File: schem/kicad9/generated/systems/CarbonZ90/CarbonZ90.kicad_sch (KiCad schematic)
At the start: 0 parts

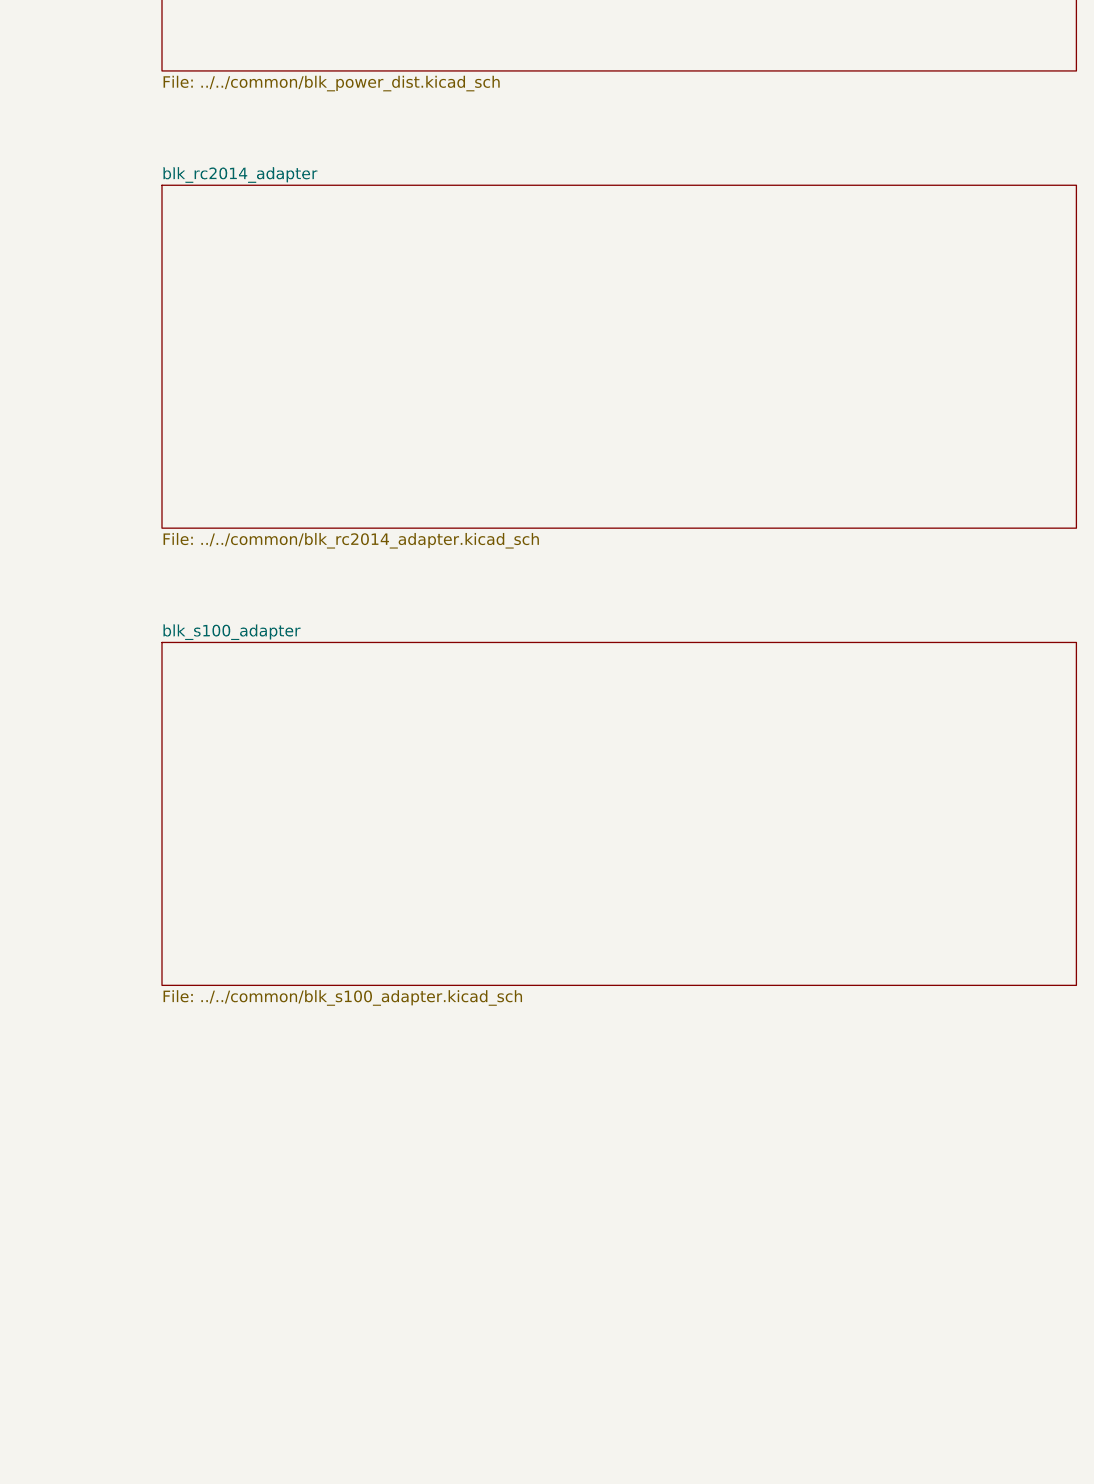
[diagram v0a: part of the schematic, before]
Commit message: kicad: add carbon block symbol library + docs + regen scripts
Detailed description:
- What was implemented: added schem/kicad9/libs/carbon_blocks.kicad_sym placeholder symbols, schem/kicad9/docs/USAGE.md, and scripts/gen_kicad.ps1 plus scripts/gen_kicad.sh; generator now embeds and uses carbon_blocks symbols in generated common block sheets and adds a JTAG/UART common block to system tops.
- Why it exists: keeps the generated hierarchy self-contained and makes regeneration repeatable while reserving a clear path to later map blocks to real parts.
- Architectural assumptions: generator overwrites only schem/kicad9/generated/; carbon_blocks symbols are placeholders (no pin-level mapping in v1); common blocks are represented as simple symbols inside common subsheets.
- How to run it: scripts/gen_kicad.ps1 or scripts/gen_kicad.sh (or python tools/kicadgen/src/kicadgen.py).
- What is NOT implemented yet: automatic mapping to specific 74ACT parts and real footprints, detailed per-net wiring between blocks, and deeper parsing of hdl/spec YAML beyond the mapping specs.
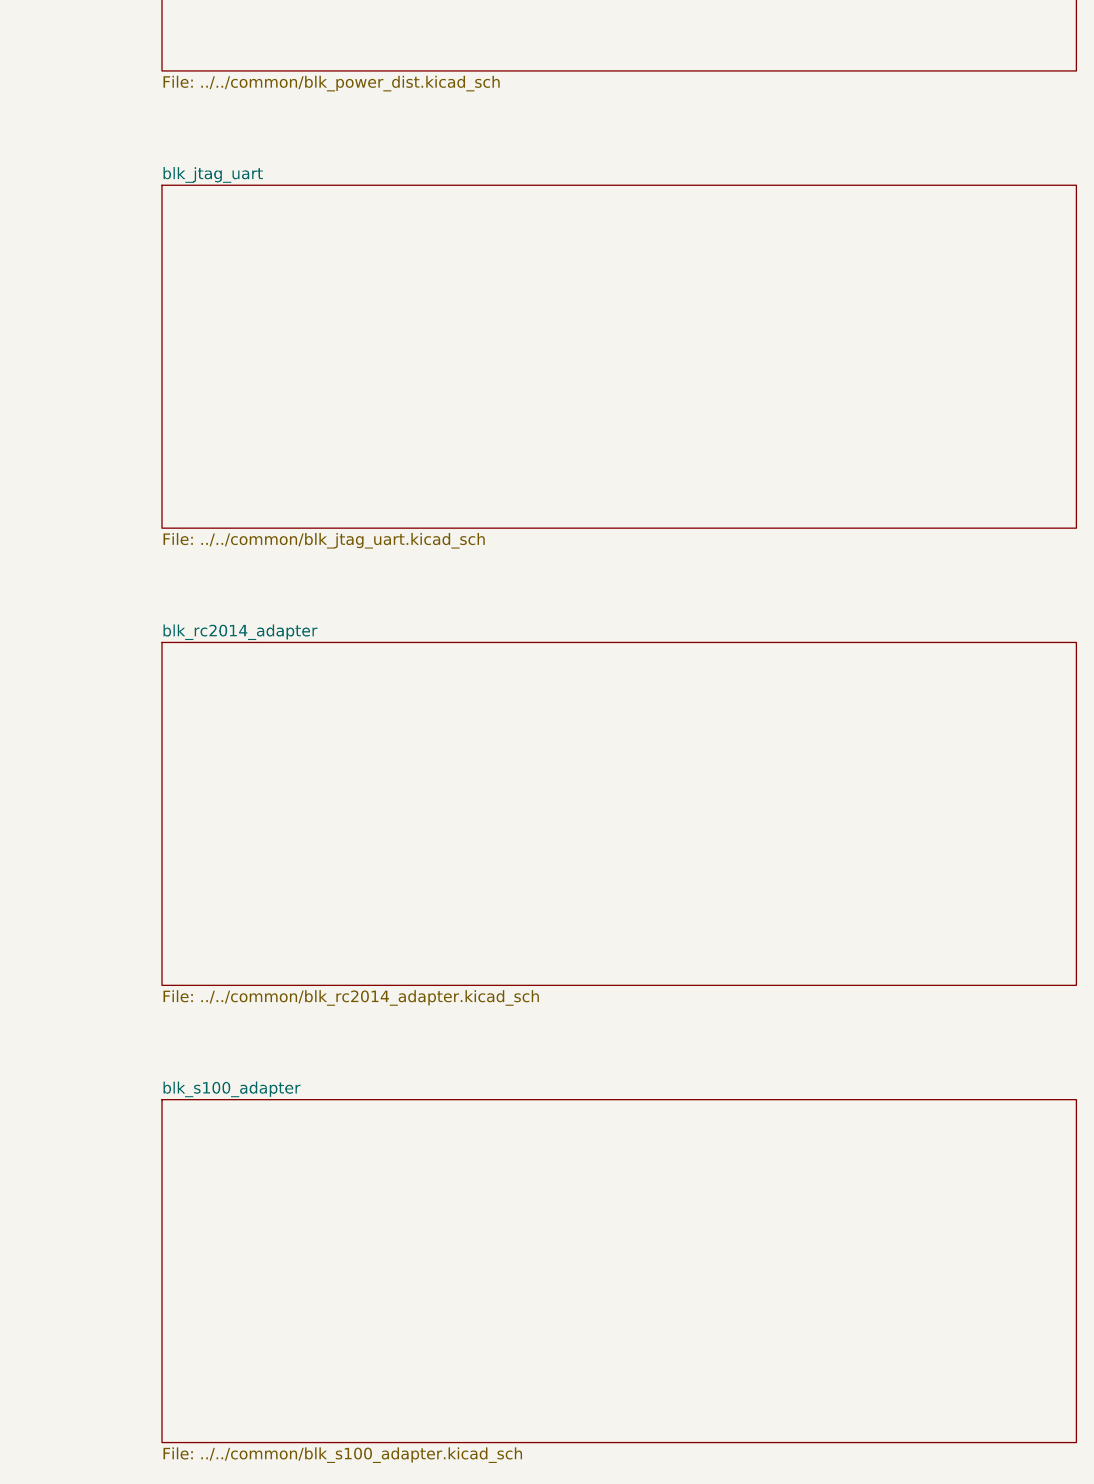
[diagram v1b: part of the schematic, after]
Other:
- added sheet blk_jtag_uart (../../common/blk_jtag_uart.kicad_sch)
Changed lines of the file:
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@@
 		(property
 			"Sheetname"
-			"blk_rc2014_adapter"
+			"blk_jtag_uart"
 			(at
 				139.7
@@
 		(property
 			"Sheetfile"
-			"../../common/blk_rc2014_adapter.kicad_sch"
+			"../../common/blk_jtag_uart.kicad_sch"
 			(at
 				139.7
@@
 		(property
 			"Sheetname"
-			"blk_s100_adapter"
+			"blk_rc2014_adapter"
 			(at
 				139.7
@@
 		(property
 			"Sheetfile"
-			"../../common/blk_s100_adapter.kicad_sch"
+			"../../common/blk_rc2014_adapter.kicad_sch"
 			(at
 				139.7
@@
 				)
 			)
+		)
+	)
+	(sheet
+		(at 139.7 350.52)
+		(size 101.6 38.1)
+		(exclude_from_sim no)
+		(in_bom yes)
+		(on_board yes)
+		(dnp no)
+		(stroke
+			(width 0)
+			(type solid)
+		)
+		(fill
+			(color
+				0
+				0
+				0
+				0
+			)
+		)
+		(property
+			"Sheetname"
+			"blk_s100_adapter"
+			(at
+				139.7
+				349.25
+				0
+			)
+			(effects
+				(font
+					(size 1.27 1.27)
+				)
+				(justify left)
+			)
+		)
+		(property
+			"Sheetfile"
+			"../../common/blk_s100_adapter.kicad_sch"
+			(at
+				139.7
+				389.89
+				0
+			)
+			(effects
+				(font
+					(size 1.27 1.27)
+				)
+				(justify left)
+			)
+		)
+		(instances
+			(project
+				"system_CarbonZ90"
+				(path
+					"/f2ef5a7e-a73c-548b-803c-6e0eb8288b7a"
+					(page "12")
+				)
+			)

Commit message: kicad: generate Carbon system hierarchical schematics
Detailed description:
- What changed: generated CarbonZ80/Z90/Z380/Z480 system schematics with CPU/FPU, memory, fabric, and platform blocks
- Why it changed: align system-level schematics with the final Z* lineage and Am95xx personalities
- Files/paths affected: schem/kicad9/generated/systems/CarbonZ80/CarbonZ80.kicad_sch, schem/kicad9/generated/systems/CarbonZ90/CarbonZ90.kicad_sch, schem/kicad9/generated/systems/CarbonZ380/CarbonZ380.kicad_sch, schem/kicad9/generated/systems/CarbonZ480/CarbonZ480.kicad_sch
- How to run it: scripts/gen_kicad.sh (or python tools/kicadgen/src/kicadgen.py)
- What remains TODO: update generator docs and add consistency checks for schematic outputs
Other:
- added sheet blk_CarbonDMA (../../cores/CarbonDMA/CarbonDMA.kicad_sch)
- added sheet blk_CarbonIO (../../cores/CarbonIO/CarbonIO.kicad_sch)
- added sheet blk_fabric (../../common/blk_fabric.kicad_sch)
- added sheet blk_mmio (../../common/blk_mmio.kicad_sch)
- sheet blk_accel: file ../../cores/Am9513/Am9513.kicad_sch -> ../../cores/Am95xx/Am95xx.kicad_sch
- sheet blk_cpu ports: added none; removed CAI_CMD[31:0], CAI_CMD_READY, CAI_CMD_VALID, CAI_RSP[31:0], CAI_RSP_READY, CAI_RSP_VALID
